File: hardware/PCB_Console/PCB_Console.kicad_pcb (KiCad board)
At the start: 2 copper layers, 165 x 150 mm, 50 parts, among them J1 USB_C_Receptacle_PowerOnly_6P, J2 CP2102 module, Q1 2N3904, U1 LD1117S33TR_SOT223, U2 IP5306, U3 ESP32-WROOM-32

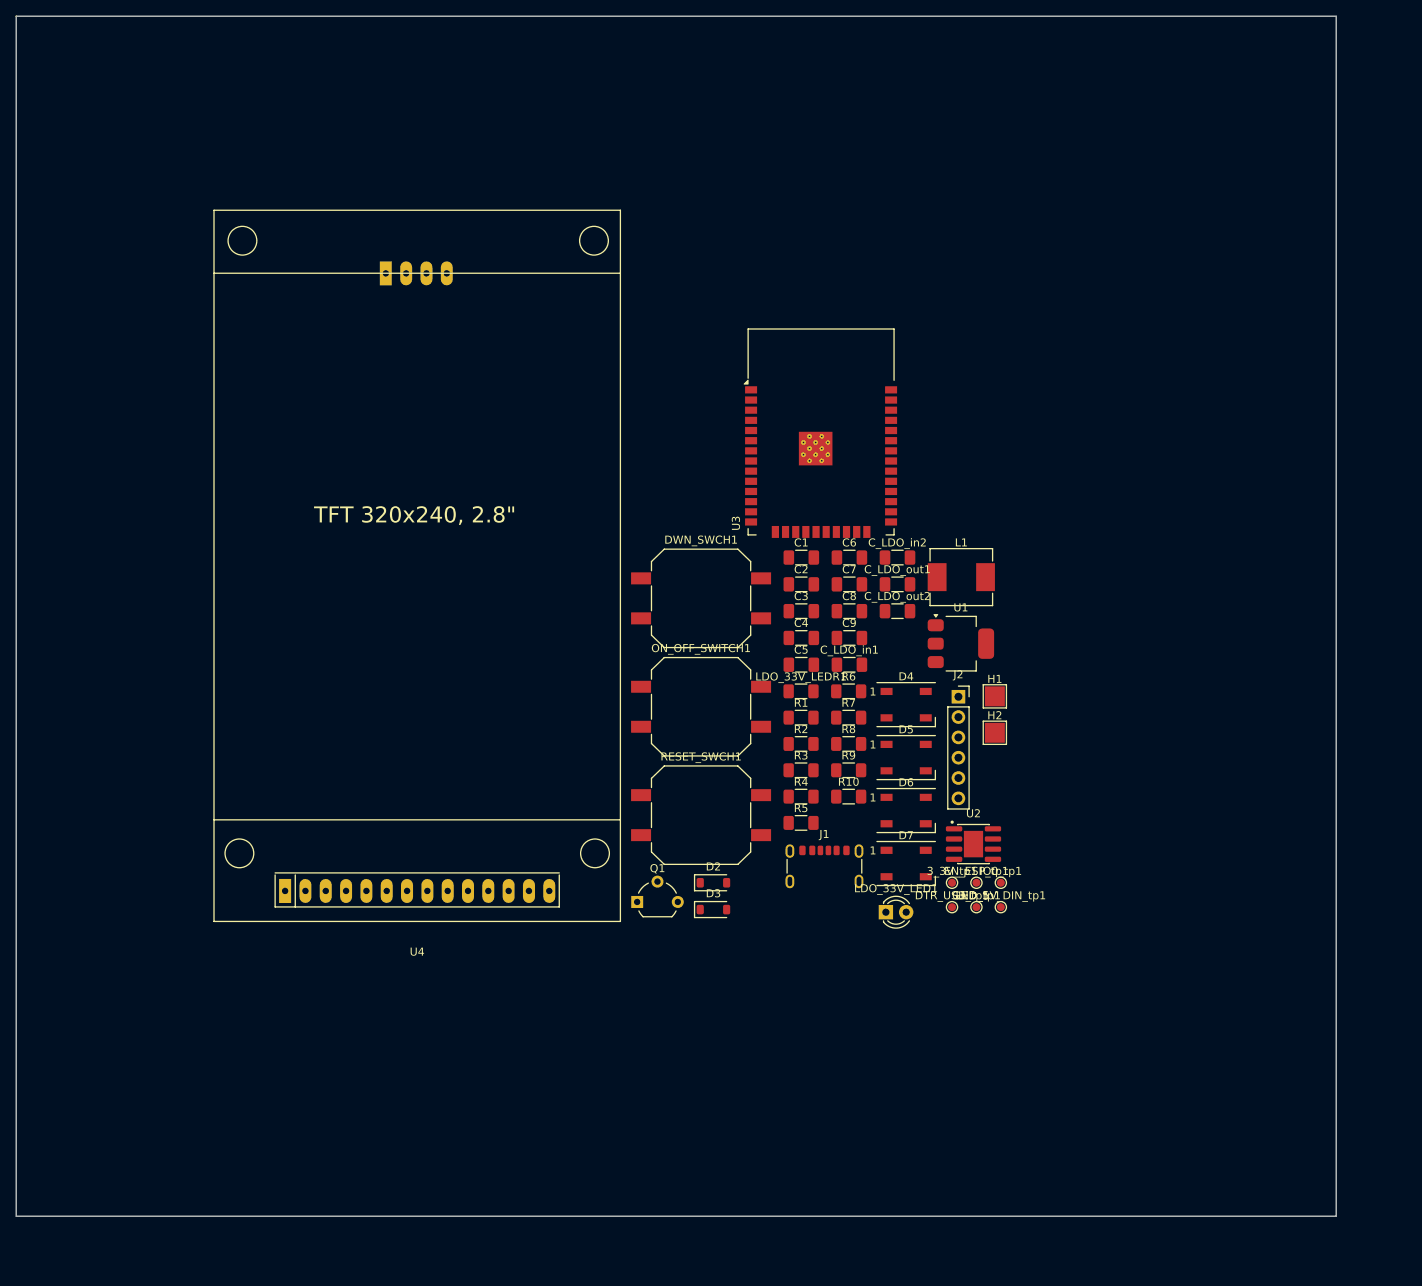
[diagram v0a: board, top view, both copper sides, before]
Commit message: dodano przyciski, poprawione biblioteki
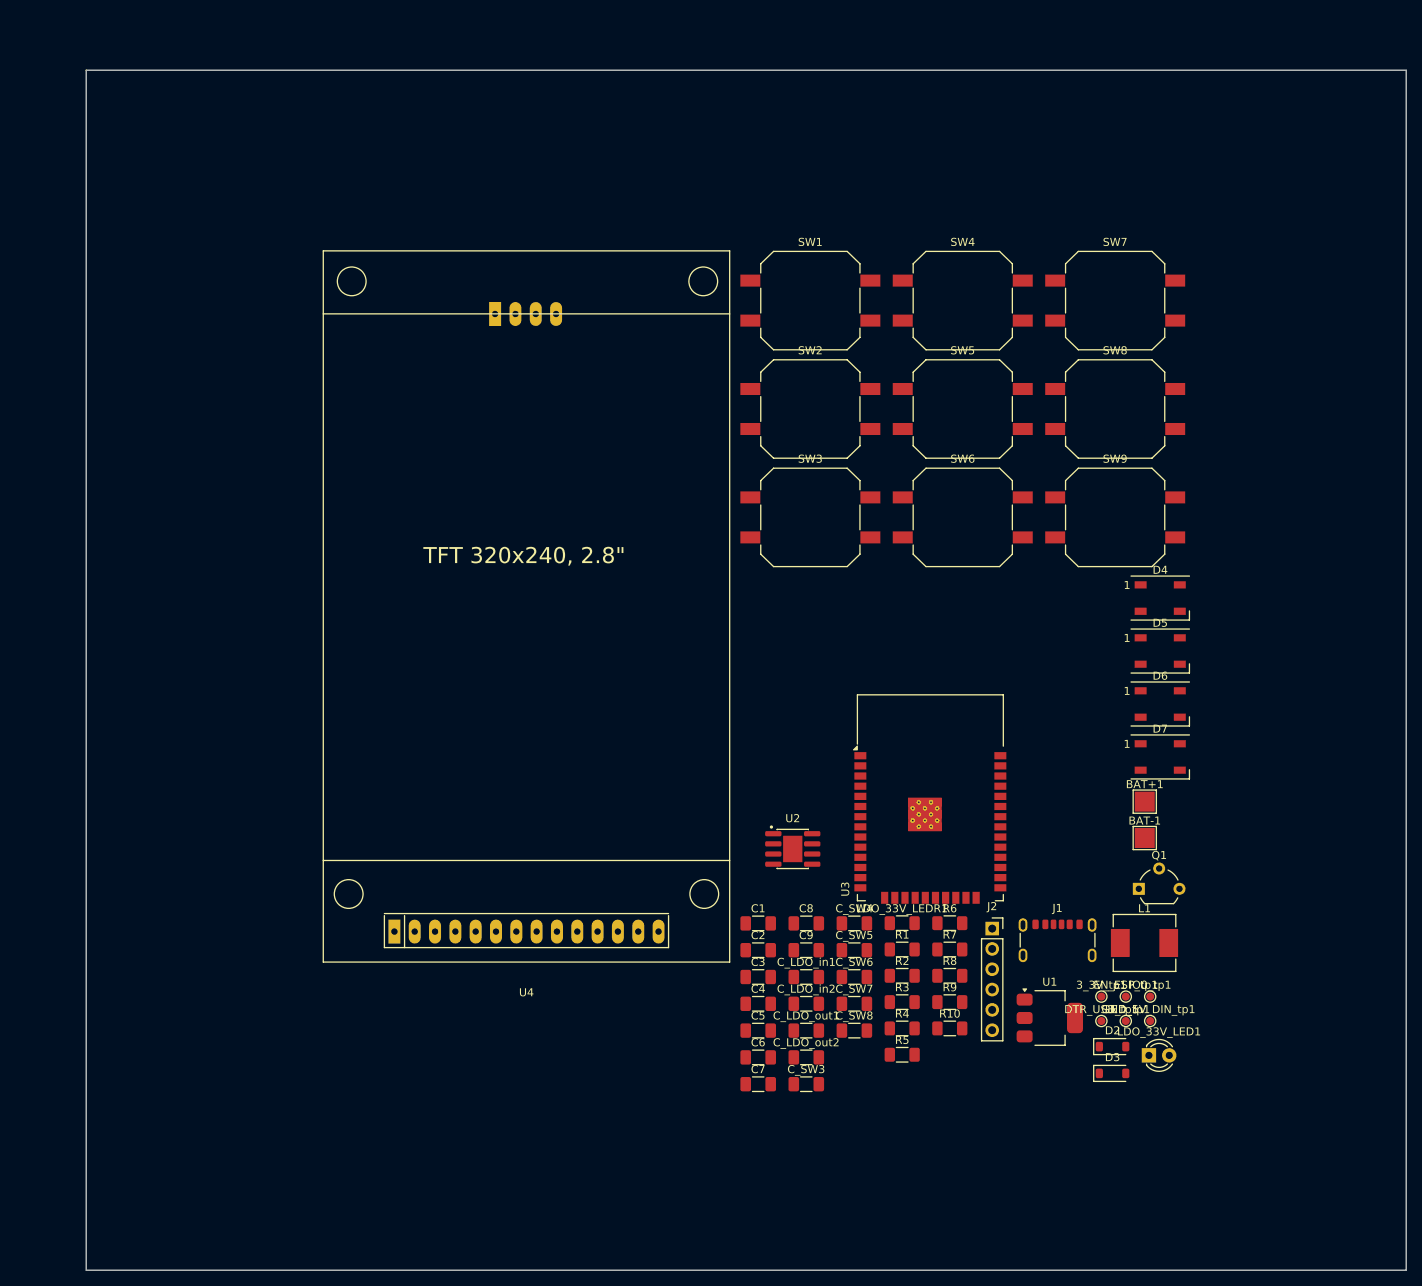
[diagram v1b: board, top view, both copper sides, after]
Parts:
- removed DWN_SWCH1, ON_OFF_SWITCH1, RESET_SWCH1: SW_Push_Dual, Library:SW_Push_12x12_aliexpress
- removed H1, H2: MountingHole_Pad_MP, TestPoint:TestPoint_Pad_2.5x2.5mm
- added BAT+1: MountingHole_Pad_MP, TestPoint:TestPoint_Pad_2.5x2.5mm, F.Cu at (256.8, 161.4)
- added BAT-1: MountingHole_Pad_MP, TestPoint:TestPoint_Pad_2.5x2.5mm, F.Cu at (256.8, 166.0)
- added C_SW3: 100n, Capacitor_SMD:C_1206_3216Metric_Pad1.33x1.80mm_HandSolder, F.Cu at (214.5, 196.7)
- added C_SW4: 100n, Capacitor_SMD:C_1206_3216Metric_Pad1.33x1.80mm_HandSolder, F.Cu at (220.5, 176.6)
- added C_SW5: 100n, Capacitor_SMD:C_1206_3216Metric_Pad1.33x1.80mm_HandSolder, F.Cu at (220.5, 180.0)
- added C_SW6: 100n, Capacitor_SMD:C_1206_3216Metric_Pad1.33x1.80mm_HandSolder, F.Cu at (220.5, 183.3)
- added C_SW7: 100n, Capacitor_SMD:C_1206_3216Metric_Pad1.33x1.80mm_HandSolder, F.Cu at (220.5, 186.7)
- added C_SW8: 100n, Capacitor_SMD:C_1206_3216Metric_Pad1.33x1.80mm_HandSolder, F.Cu at (220.5, 190.0)
- added SW1: SW_MEC_5E, Library:SW_Push_12x12_aliexpress, F.Cu at (215.0, 98.8)
- added SW2: SW_MEC_5E, Library:SW_Push_12x12_aliexpress, F.Cu at (215.0, 112.3)
- added SW3: SW_MEC_5E, Library:SW_Push_12x12_aliexpress, F.Cu at (215.0, 125.9)
- added SW4: SW_MEC_5E, Library:SW_Push_12x12_aliexpress, F.Cu at (234.1, 98.8)
- added SW5: SW_MEC_5E, Library:SW_Push_12x12_aliexpress, F.Cu at (234.1, 112.3)
- added SW6: SW_MEC_5E, Library:SW_Push_12x12_aliexpress, F.Cu at (234.1, 125.9)
- added SW7: SW_MEC_5E, Library:SW_Push_12x12_aliexpress, F.Cu at (253.1, 98.8)
- added SW8: SW_MEC_5E, Library:SW_Push_12x12_aliexpress, F.Cu at (253.1, 112.3)
- added SW9: SW_MEC_5E, Library:SW_Push_12x12_aliexpress, F.Cu at (253.1, 125.9)
- R10: value 10k -> 0R
- R6: value 0R -> 1k
- R7: value 1k -> 330
- R8: value 330 -> 10k
- U2: footprint IP5306:SOIC9P127_490X600X170L84X42T330X241N -> components_lib:SOIC9P127_490X600X170L84X42T330X241N
- U4: footprint ASK:TFT ILI9341 -> components_lib:TFT ILI9341
- moved C6 63.5 mm to (208.5, 193.4)
- moved C7 63.5 mm to (208.5, 196.7)
- moved Q1 62.7 mm to (256.1, 172.3)
- moved C_LDO_in2 56.9 mm to (214.5, 186.7)
- moved C_LDO_out1 56.9 mm to (214.5, 190.0)
- moved C_LDO_out2 56.9 mm to (214.5, 193.4)
- moved D2 53.9 mm to (252.8, 192.0)
- moved D3 53.9 mm to (252.8, 195.4)
- moved L1 51.1 mm to (256.8, 179.1)
- moved U1 48.1 mm to (244.9, 188.5)
- moved U3 47.7 mm to (230.0, 163.9)
- moved C3 46.0 mm to (208.5, 183.3)
- moved C4 46.0 mm to (208.5, 186.7)
- moved C1 46.0 mm to (208.5, 176.6)
- moved C2 46.0 mm to (208.5, 180.0)
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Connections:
- R10 pad 1: 3_3V_AMSVO -> Net-(C8-Pad2)
- R10 pad 2: EN_ESP -> DTR_BL
- R6 pad 1: Net-(C8-Pad2) -> IC_LED_DIN
- R6 pad 2: DTR_BL -> Net-(Q1-B)
- R7 pad 1: IC_LED_DIN -> Net-(Q1-C)
- R7 pad 2: Net-(Q1-B) -> Net-(D4-DIN)
- R8 pad 1: Net-(Q1-C) -> 3_3V_AMSVO
- R8 pad 2: Net-(D4-DIN) -> GPIO0
- R9 pad 2: GPIO0 -> EN_ESP
- U3 pad 10: unconnected-(U3-IO25-Pad10) -> IO25_B
- U3 pad 11: unconnected-(U3-IO26-Pad11) -> IO26_B
- U3 pad 12: unconnected-(U3-IO27-Pad12) -> IO27_B
- U3 pad 13: unconnected-(U3-IO14-Pad13) -> IO14_B
- U3 pad 8: unconnected-(U3-IO32-Pad8) -> IO32_B
- U3 pad 9: unconnected-(U3-IO33-Pad9) -> IO33_B

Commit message: zaczynam routing, zaczynam sie martwic ze ten projekt jest awykonalny w dostepnej technologi
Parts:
- added D1: BLUE, LED_THT:LED_D5.0mm, F.Cu at (303.8, 203.2)
- added Q2: 2N3904, Package_TO_SOT_THT:TO-92_Wide, F.Cu at (302.9, 196.9)
- added R11: 1k, Resistor_SMD:R_1206_3216Metric_Pad1.30x1.75mm_HandSolder, F.Cu at (311.8, 201.1)
- moved D6 222.0 mm to (55.5, 59.8)
- moved D7 216.7 mm to (64.4, 59.8)
- moved D5 216.3 mm to (55.5, 68.5)
- moved SW9 210.5 mm to (63.5, 34.5)
- moved J1 210.3 mm to (100.0, 28.4), turned to 180 degrees
- moved D4 205.6 mm to (64.4, 68.6)
- moved SW5 169.6 mm to (69.0, 151.5)
- moved U2 166.5 mm to (116.2, 31.8), turned to 180 degrees
- moved SW7 165.7 mm to (96.0, 151.5)
- moved SW4 156.8 mm to (82.5, 139.0)
- moved SW6 156.3 mm to (82.5, 164.0)
- moved U1 137.0 mm to (135.5, 106.0), turned to -90 degrees
- moved SW8 120.2 mm to (139.5, 151.5)
- moved U3 116.2 mm to (142.1, 87.9), turned to -90 degrees
- moved J2 113.9 mm to (136.3, 125.5), turned to 90 degrees
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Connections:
- C_SW6 pad 2: IO26_B -> IO34_B
- C_SW7 pad 2: IO25_B -> IO35_B
- SW6 pad 1: IO26_B -> IO34_B
- SW6 pad 2: IO26_B -> IO34_B
- SW7 pad 1: IO25_B -> IO35_B
- SW7 pad 2: IO25_B -> IO35_B
- U3 pad 10: IO25_B -> SPI_CS_SD
- U3 pad 11: IO26_B -> IC_LED_DIN
- U3 pad 16: unconnected-(U3-IO13-Pad16) -> T_IRQ
- U3 pad 26: unconnected-(U3-IO4-Pad26) -> SPI_CS_T
- U3 pad 27: unconnected-(U3-IO16-Pad27) -> D_DC
- U3 pad 28: unconnected-(U3-IO17-Pad28) -> D_RST
- U3 pad 30: unconnected-(U3-IO18-Pad30) -> SPI_SCK
- U3 pad 31: unconnected-(U3-IO19-Pad31) -> SPI_MISO
- U3 pad 33: unconnected-(U3-IO21-Pad33) -> SPI_CS_D
- U3 pad 34: TXD -> TXD_USB
- U3 pad 35: RXD -> RXD_USB
- U3 pad 36: unconnected-(U3-IO22-Pad36) -> DLED_PWM
- U3 pad 37: unconnected-(U3-IO23-Pad37) -> SPI_MOSI
- U3 pad 6: unconnected-(U3-IO34-Pad6) -> IO34_B
- U3 pad 7: IC_LED_DIN -> IO35_B
- U4 pad 1: 5V_USB_BL -> 3_3V_AMSVO
- U4 pad 10: unconnected-(U4-T_CLK-Pad10) -> SPI_SCK
- U4 pad 11: unconnected-(U4-T_CS-Pad11) -> SPI_CS_T
- U4 pad 12: unconnected-(U4-T_DIN-Pad12) -> SPI_MOSI
- U4 pad 13: unconnected-(U4-T_DO-Pad13) -> SPI_MISO
- U4 pad 14: unconnected-(U4-T_IRQ-Pad14) -> T_IRQ
- U4 pad 15: unconnected-(U4-SD_CS-Pad15) -> SPI_CS_SD
- U4 pad 16: unconnected-(U4-SD_MOSI-Pad16) -> SPI_MOSI
- U4 pad 17: unconnected-(U4-SD_NISO-Pad17) -> SPI_MISO
- U4 pad 18: unconnected-(U4-SD_SCK-Pad18) -> SPI_SCK
- U4 pad 3: unconnected-(U4-CS-Pad3) -> SPI_CS_D
- U4 pad 4: unconnected-(U4-RESET-Pad4) -> D_RST
- U4 pad 5: unconnected-(U4-DC-Pad5) -> D_DC
- U4 pad 6: unconnected-(U4-SDI-Pad6) -> SPI_MOSI
- U4 pad 7: unconnected-(U4-SCK-Pad7) -> SPI_SCK
- U4 pad 8: unconnected-(U4-LED-Pad8) -> D_LED
- U4 pad 9: unconnected-(U4-SDO-Pad9) -> SPI_MISO
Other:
- board size 165 x 150 mm -> 100 x 150 mm

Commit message: routing and placment, few edits on schematics
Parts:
- removed 3_3V_tp1, IO0_tp1: TestPoint, TestPoint:TestPoint_Pad_D1.0mm
- removed BAT+1, BAT-1: MountingHole_Pad_MP, TestPoint:TestPoint_Pad_2.5x2.5mm
- added TP2: Battery-, TestPoint:TestPoint_THTPad_D1.5mm_Drill0.7mm, F.Cu at (53.5, 77.0)
- added TP3: Battery+, TestPoint:TestPoint_THTPad_D1.5mm_Drill0.7mm, F.Cu at (53.5, 83.5)
- GND_tp1: footprint TestPoint:TestPoint_Pad_D1.0mm -> TestPoint:TestPoint_Pad_D1.5mm
- moved LED_5V_DIN_tp1 292.9 mm to (69.5, 47.5)
- moved R4 287.8 mm to (52.5, 34.5), turned to -90 degrees
- moved Q1 279.4 mm to (71.0, 55.8)
- moved L1 274.9 mm to (69.0, 81.0)
- moved D1 273.1 mm to (54.0, 93.0), turned to 90 degrees
- moved D2 272.6 mm to (96.5, 37.5)
- moved R7 268.0 mm to (64.4, 54.0)
- moved R6 256.7 mm to (72.0, 61.0)
- moved R1 254.9 mm to (60.0, 82.0)
- moved R2 254.9 mm to (60.0, 85.3)
- moved R5 251.2 mm to (59.5, 107.0)
- moved R3 242.7 mm to (103.0, 37.5)
- moved C9 240.6 mm to (70.0, 68.5), turned to 90 degrees
- moved C1 238.7 mm to (60.0, 78.0)
- moved C6 237.6 mm to (59.4, 98.6)
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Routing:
- net Bat-: track 0.00 -> 41.0 mm
- net 5V_USB_BL: track 0.00 -> 8.66 mm
- net DTR_BL: track 0.00 -> 7.30 mm
- net 3_3V_AMSVO: track 0.00 -> 7.16 mm
- net IO34_B: track 0.00 -> 6.71 mm
- net IO32_B: track 0.00 -> 5.39 mm
- net IO14_B: track 0.00 -> 5.39 mm
- net EN_ESP: track 0.00 -> 5.03 mm
- net IO33_B: track 0.00 -> 4.89 mm
- net IO27_B: track 0.00 -> 3.89 mm
- net Net-(LDO_33V_LED1-K): track 0.00 -> 3.66 mm
- net IO35_B: track 0.00 -> 3.39 mm
- net Net-(C8-Pad2): track 0.00 -> 2.89 mm

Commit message: routing next step
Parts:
- removed EN_ESP_tp1: TestPoint, TestPoint:TestPoint_Pad_D1.0mm
- removed R10: 0R, Resistor_SMD:R_1206_3216Metric_Pad1.30x1.75mm_HandSolder
- added R12: 0, Resistor_SMD:R_1206_3216Metric_Pad1.30x1.75mm_HandSolder, F.Cu at (119.4, 107.2)
- added R13: 0, Resistor_SMD:R_1206_3216Metric_Pad1.30x1.75mm_HandSolder, F.Cu at (145.6, 106.8)
- D2, D3: footprint Diode_SMD:D_SOD-123 -> Diode_SMD:D_0805_2012Metric_Pad1.15x1.40mm_HandSolder
- SW1, SW2: footprint Library:SW_Push_12x12_aliexpress -> TS04-66-95-BK-100-SMT:SW_TS04-66-95-BK-100-SMT
- moved DTR_USB_tp1 108.7 mm to (130.0, 28.6)
- moved R8 41.7 mm to (127.4, 105.3), turned to 90 degrees
- moved R9 16.9 mm to (136.2, 71.4), turned to -90 degrees
- moved SW1 12.5 mm to (138.9, 47.0), turned to 180 degrees
- moved SW2 12.3 mm to (139.0, 35.2), turned to 180 degrees
- moved C8 9.72 mm to (129.2, 39.1)
- moved R11 2.68 mm to (119.6, 127.6)
- moved U4 1.86 mm to (99.8, 122.0)
- moved J2 0.90 mm to (111.8, 34.6)
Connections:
- C8 pad 2: Net-(C8-Pad2) -> DTR_BL
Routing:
- net Bat-: track 41.0 -> 270.9 mm
- net 3_3V_AMSVO: track 7.16 -> 128.0 mm
- net IO32_B: track 5.39 -> 89.0 mm
- net EN_ESP: track 5.03 -> 59.2 mm
- net DLED_PWM: track 0.00 -> 51.6 mm
- net DTR_BL: track 7.30 -> 20.6 mm
- net D_LED: track 0.00 -> 10.7 mm
- net Net-(Q2-B): track 0.00 -> 8.65 mm
- net GPIO0: track 0.00 -> 8.19 mm
- net Net-(C8-Pad2): track 2.89 -> 0.00 mm
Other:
- board text added: "160269 160168 160232 160133"
- board text added: "ASK2025"
- board text added: "BM"
- board text added: "EN"
- board text added: "KAROL LESZYŃSKI"
- board text added: "designed and produced by"

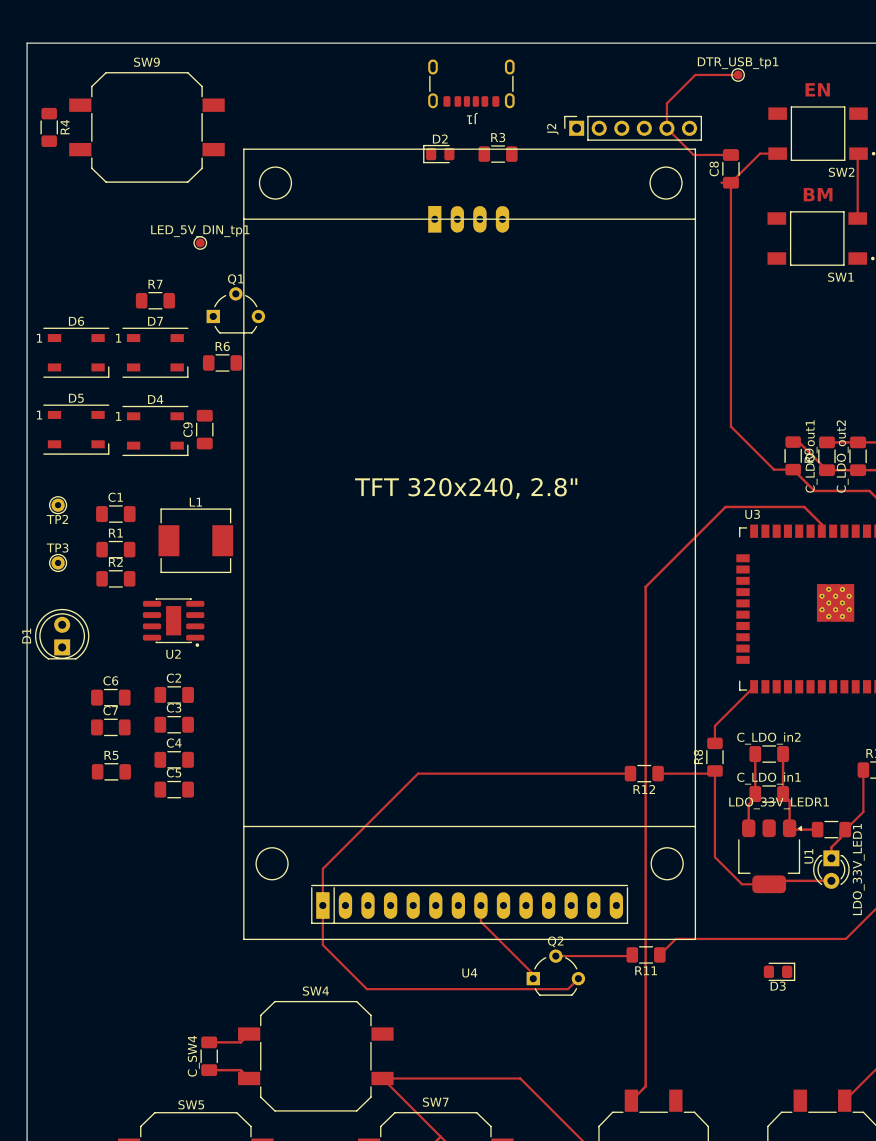
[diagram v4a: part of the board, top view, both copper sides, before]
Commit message: routing czesc dalsza, power manager system wmiare polaczony
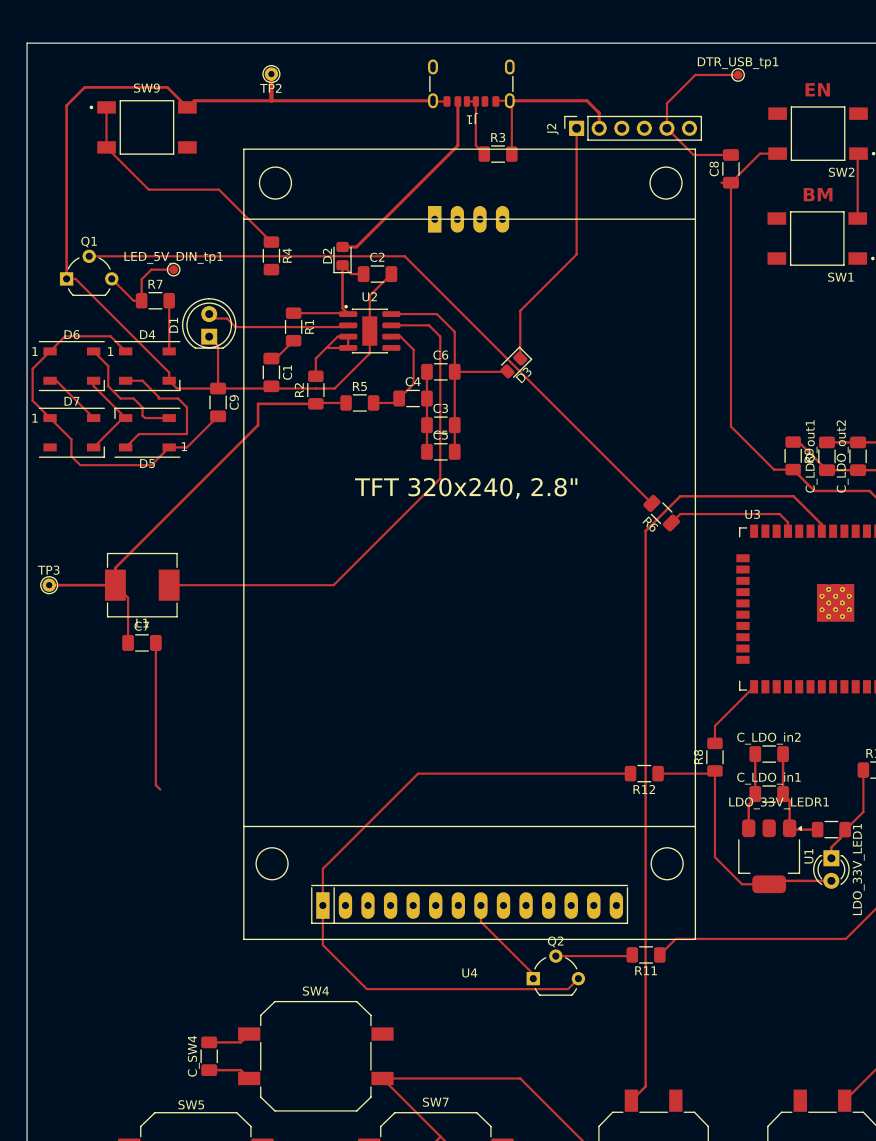
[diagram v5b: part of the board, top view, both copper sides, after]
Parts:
- SW1: footprint TS04-66-95-BK-100-SMT:SW_TS04-66-95-BK-100-SMT -> components_lib:SW_TS04-66-95-BK-100-SMT
- SW9: footprint Library:SW_Push_12x12_aliexpress -> components_lib:SW_TS04-66-95-BK-100-SMT
- moved D3 74.5 mm to (104.8, 61.2), turned to -135 degrees
- moved TP2 54.1 mm to (77.5, 28.5)
- moved C2 52.6 mm to (89.4, 51.0)
- moved R6 52.2 mm to (121.4, 77.9), turned to 135 degrees
- moved C6 52.2 mm to (96.6, 62.0)
- moved R5 50.0 mm to (87.4, 65.5)
- moved C4 48.7 mm to (93.4, 65.0)
- moved C5 48.4 mm to (96.6, 71.0)
- moved C3 45.1 mm to (96.6, 68.0)
- moved U2 39.4 mm to (88.6, 57.4), turned to 0 degrees
- moved D1 38.7 mm to (70.5, 58.0)
- moved R1 32.1 mm to (80.0, 56.9), turned to -90 degrees
- moved R2 30.9 mm to (82.5, 64.0), turned to 90 degrees
- moved R4 28.9 mm to (77.5, 48.9)
- moved C1 23.7 mm to (77.5, 62.0), turned to -90 degrees
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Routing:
- net Bat-: track 270.9 -> 452.6 mm
- net Net-(Q1-B): track 0.00 -> 74.8 mm
- net 5V_USB_BL: track 8.66 -> 80.7 mm
- net Net-(U2-SW): track 0.00 -> 57.5 mm
- net Bat+: track 0.00 -> 51.5 mm
- net Net-(R4-Pad1): track 0.00 -> 27.5 mm
- net Net-(D3-A): track 0.00 -> 27.4 mm
- net Net-(D2-A): track 0.00 -> 22.7 mm
- net Net-(D4-DOUT): track 0.00 -> 18.8 mm
- net Net-(D1-A): track 0.00 -> 16.3 mm
- net IC_LED_DIN: track 0.00 -> 14.9 mm
- net 5V_USB_C: track 0.00 -> 14.7 mm
- net Net-(D5-DOUT): track 0.00 -> 13.5 mm
- net Net-(U2-BAT): track 0.00 -> 12.4 mm
- net Net-(Q1-C): track 0.00 -> 10.8 mm
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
